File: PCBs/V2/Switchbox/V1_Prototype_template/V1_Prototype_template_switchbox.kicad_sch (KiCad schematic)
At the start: 9 parts, among them J3(IN)1 01x04 magnetic connector, J5(OUT)1 01x04 magnetic connector

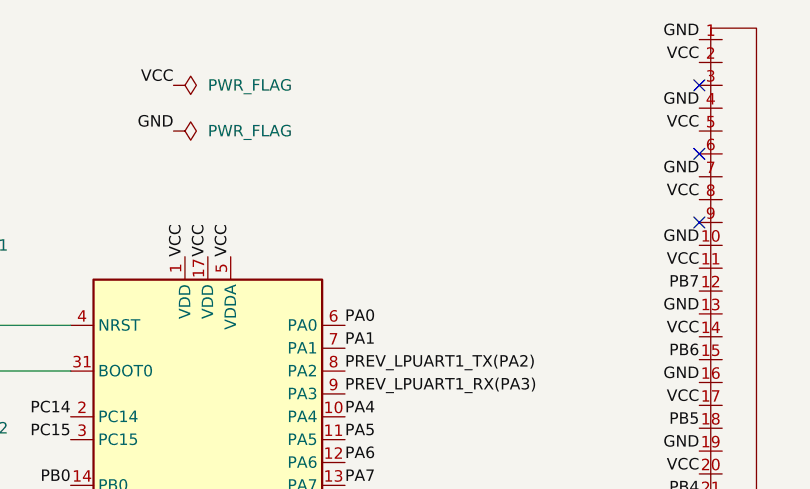
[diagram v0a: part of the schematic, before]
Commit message: testing and fixing PCBs, reordered
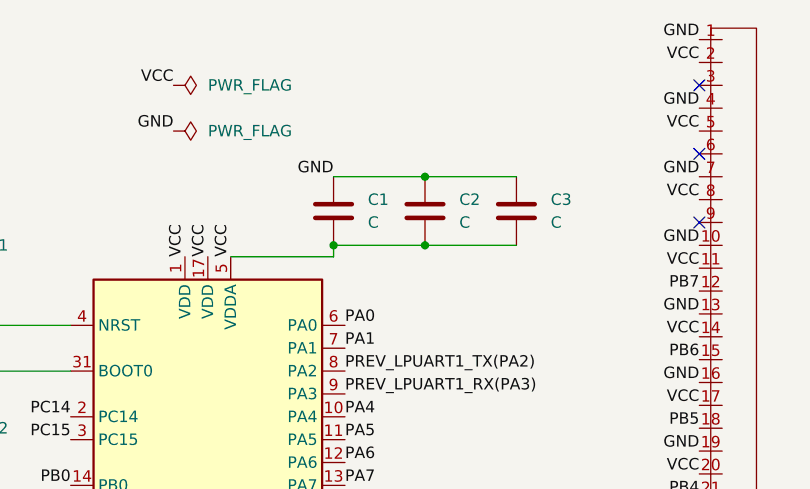
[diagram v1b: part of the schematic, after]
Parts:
- added C1, C2, C3: C, Capacitor_SMD:C_0603_1608Metric, symbol Device:C
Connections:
- net GND: now also C1.1, C2.1, C3.1
- net VCC: now also C1.2, C2.2, C3.2
